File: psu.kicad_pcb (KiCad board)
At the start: 2 copper layers, 76.2 x 76.2 mm, 69 parts, among them J1 Screw_Terminal_01x02, J2 Barrel_Jack, J3 Binding posts, SW1 SW_SP4T, SW2 SW_SP4T, SW3 Lever toggle, U1 LM4040DBZ-2.5, U2 LT3081, U3 LM393, U4 LM334M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

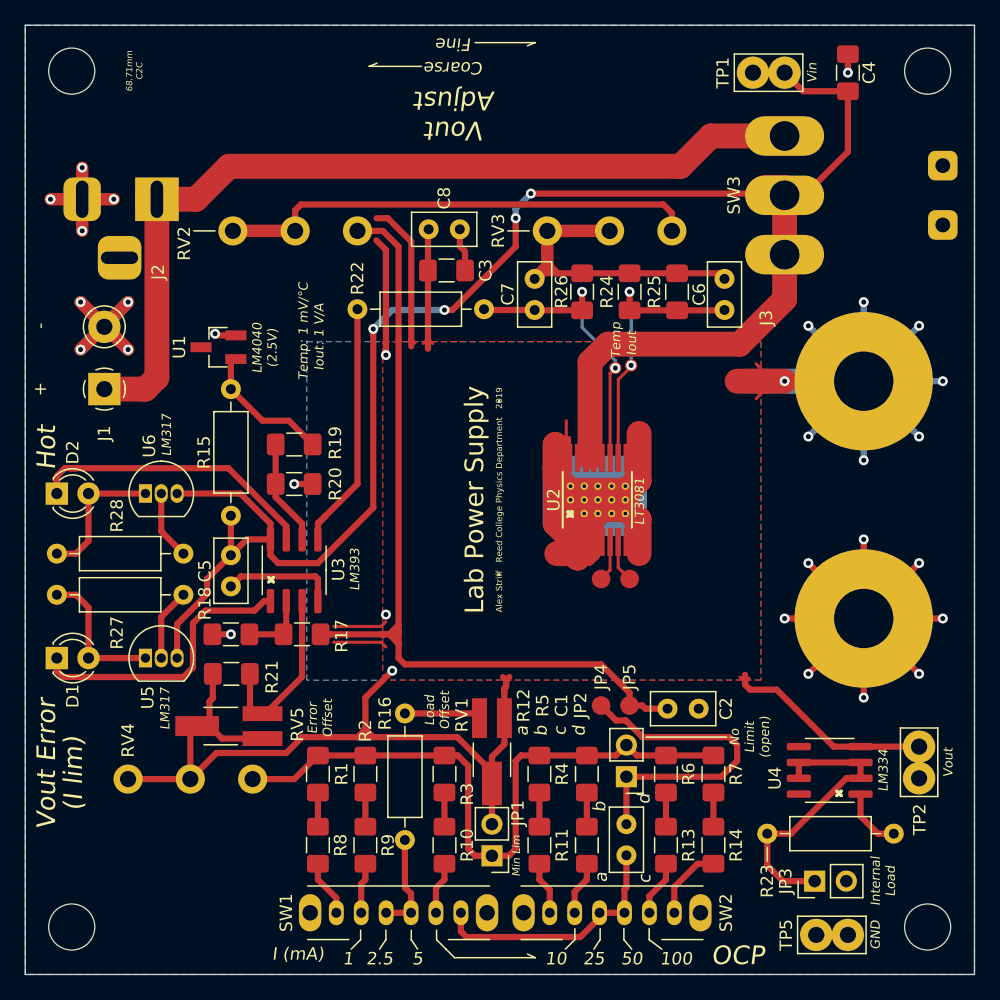
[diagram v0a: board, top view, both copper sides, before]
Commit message: Cleaned up silkscreen
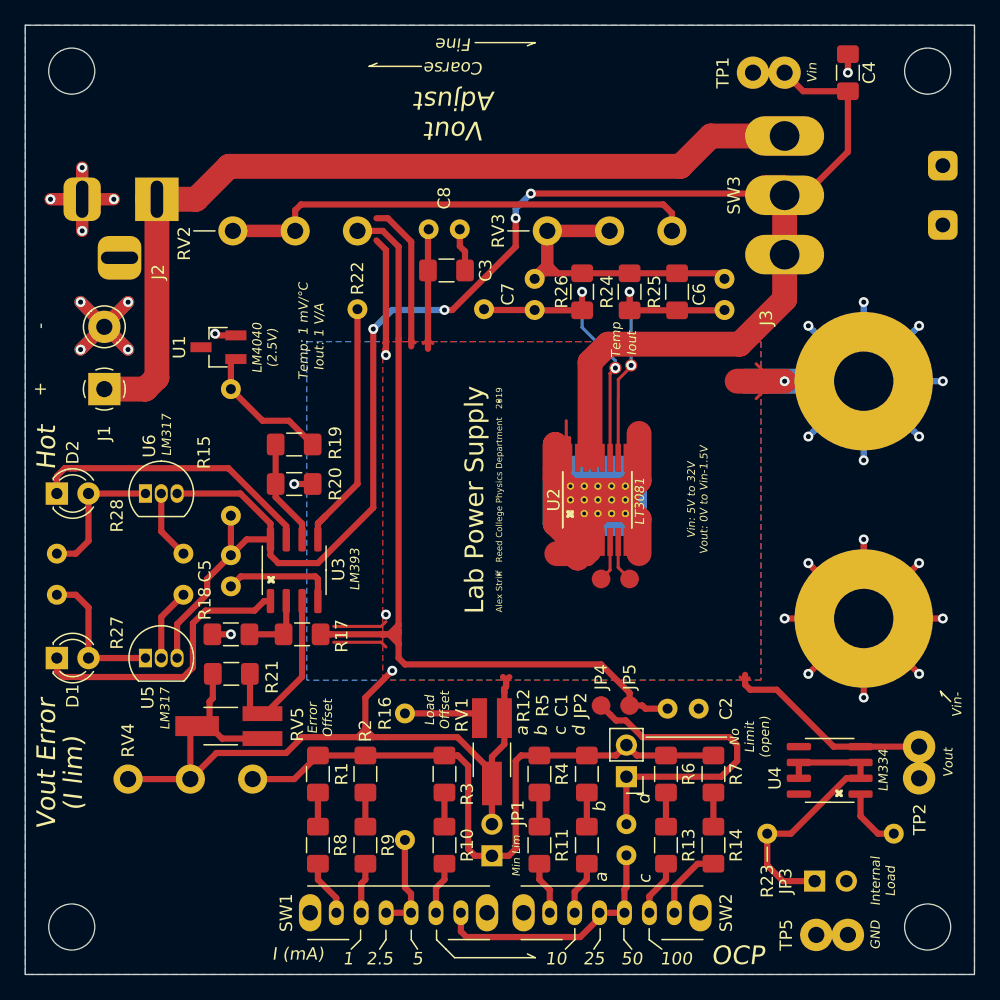
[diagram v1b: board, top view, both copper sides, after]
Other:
- board text added: "Vin-"
- board text added: "Vin: 5V to 32V Vout: 0V to Vin-1.5V"
- board text removed: "68.71mm C2C"

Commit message: Final changes before manufacture
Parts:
- moved C2 0.84 mm to (153.9, 114.8)
- turned J3 to 90 degrees
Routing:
- net Vout: track 313.0 -> 279.4 mm
- net Vin: track 151.6 -> 135.6 mm, vias 4 -> 2
- net GND: track 126.7 -> 119.6 mm, vias 20 -> 21
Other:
- board text removed: "Vin-"

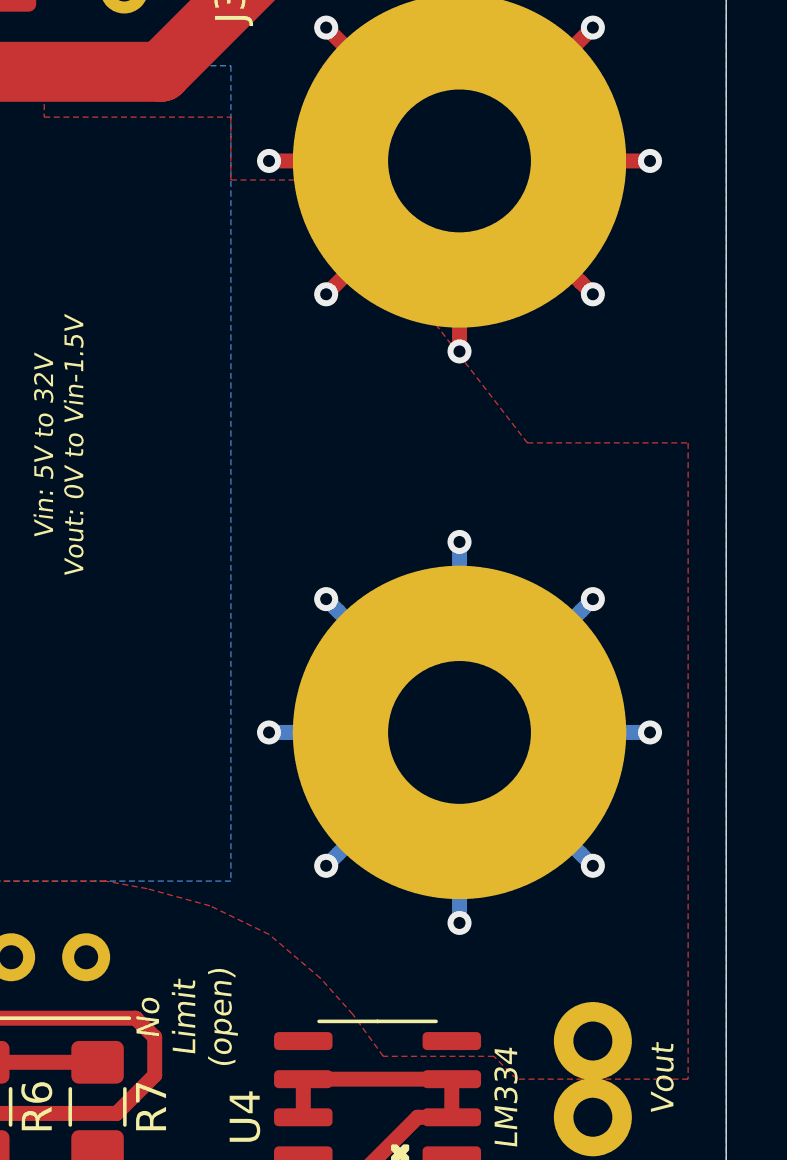
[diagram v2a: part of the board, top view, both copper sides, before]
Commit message: Minor tweak to Vout fill; add gerbers
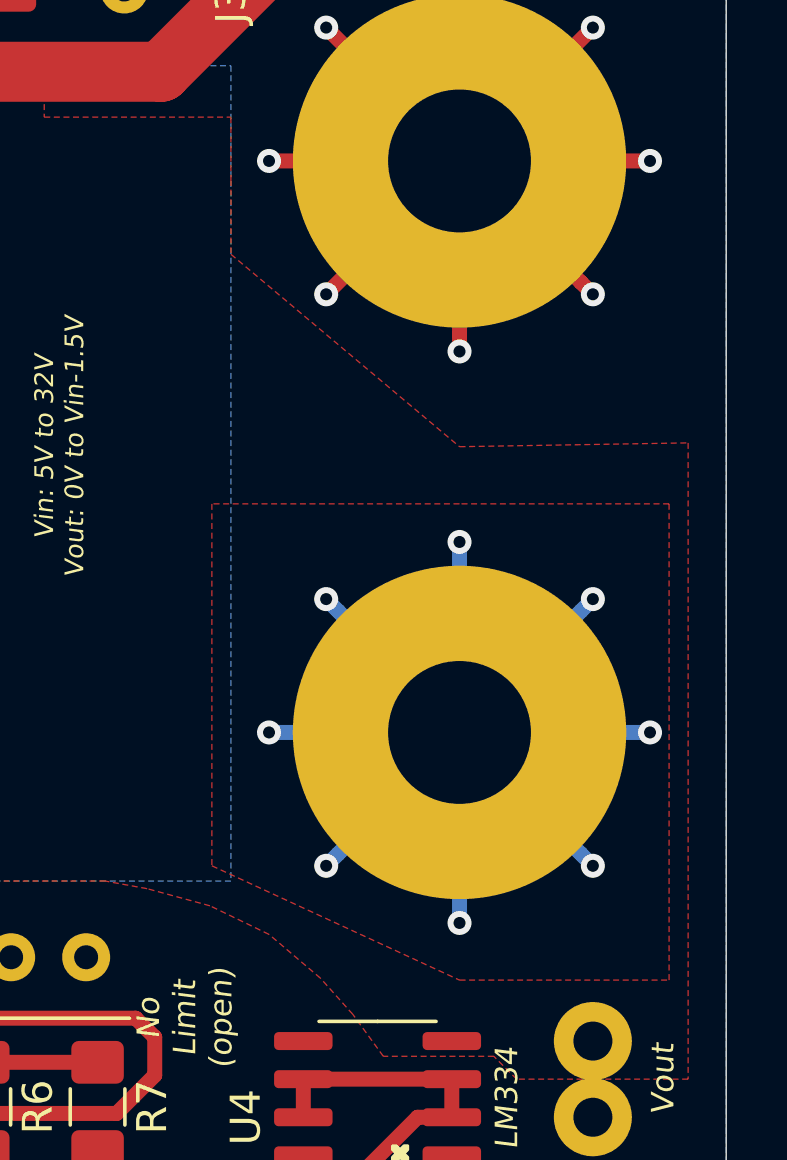
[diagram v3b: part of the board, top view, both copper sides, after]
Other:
- board text added: "NOTES Material: 1.6 mm FR4 (standard); 1 oz copper; 2 layers. Board dimensions: 3 in x 3 in. Colors: White solder mask, black silk screen (front). Surface finish: HASL (with lead) (standard). NO gold fingers NO panelization NO castellated holes NO tented vias NO stencil"
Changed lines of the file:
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@@
   (general
     (thickness 1.6)
-    (drawings 106)
+    (drawings 107)
     (tracks 507)
     (zones 0)
@@
     (visible_elements 7FFFFFFF)
     (pcbplotparams
-      (layerselection 0x010fc_ffffffff)
+      (layerselection 0x012f0_ffffffff)
       (usegerberextensions false)
       (usegerberattributes false)
@@
       (outputformat 1)
       (mirror false)
-      (drillshape 1)
+      (drillshape 0)
       (scaleselection 1)
-      (outputdirectory ""))
+      (outputdirectory "gerbers/"))
   )
   (net 0 "")
@@
     )
   )
+  (gr_text "NOTES\n\nMaterial: 1.6 mm FR4 (standard); 1 oz copper; 2 layers.\nBoard dimensions: 3 in x 3 in.\nColors: White solder mask, black silk screen (front).\nSurface finish: HASL (with lead) (standard).\nNO gold fingers\nNO panelization\nNO castellated holes\nNO tented vias\nNO stencil\n" (at 22.86 40.64) (layer Cmts.User)
+    (effects (font (size 2 2) (thickness 0.15)) (justify left))
+  )
   (gr_circle (center 162.56 97.79) (end 163.449 97.79) (layer B.Mask) (width 0.15))
   (gr_circle (center 165.1 97.79) (end 165.1 97.663) (layer B.Mask) (width 0.15))
@@
     (min_thickness 0.254)
     (keepout (tracks allowed) (vias allowed) (copperpour not_allowed))
-    (fill (arc_segments 32) (thermal_gap 0.508) (thermal_bridge_width 0.508) (smoothing fillet) (radius 2.54))
+    (fill (arc_segments 32) (thermal_gap 0.508) (thermal_bridge_width 0.508))
     (polygon
       (pts
-        (xy 173.99 88.265) (xy 173.99 80.645) (xy 158.75 80.645) (xy 158.75 97.663) (xy 173.99 97.663)
+        (xy 173.99 88.265) (xy 173.99 80.645) (xy 158.75 80.645) (xy 173.99 97.663)
       )
     )
   )
   (zone (net 5) (net_name Vout) (layer F.Cu) (hatch edge 0.508)
+    (priority 1)
     (connect_pads (clearance 0.508))
     (min_thickness 0.254)
-    (fill yes (arc_segments 32) (thermal_gap 0.508) (thermal_bridge_width 0.508) (smoothing fillet) (radius 1.27))
+    (fill yes (arc_segments 32) (thermal_gap 0.508) (thermal_bridge_width 0.508) (smoothing fillet) (radius 2.54))
     (polygon
       (pts
-        (xy 152.527 86.8045) (xy 158.75 86.8045) (xy 158.75 88.9) (xy 161.8615 88.9) (xy 168.628931 97.663)
+        (xy 152.527 86.8045) (xy 158.75 86.8045) (xy 158.75 88.9) (xy 158.75 91.3765) (xy 166.37 97.79)
         (xy 173.99 97.663) (xy 173.99 118.872) (xy 168.275 118.872) (xy 167.513 118.11) (xy 163.83 118.11)
         (xy 162.814 116.713) (xy 161.7345 115.5065) (xy 160.02 114.046) (xy 158.0515 113.0935) (xy 155.956 112.522)
@@
       )
     )
+  )
+  (zone (net 5) (net_name Vout) (layer F.Cu) (hatch edge 0.508)
+    (priority 1)
+    (connect_pads yes (clearance 0.508))
+    (min_thickness 0.254)
+    (fill yes (arc_segments 32) (thermal_gap 0.508) (thermal_bridge_width 0.508))
+    (polygon
+      (pts
+        (xy 166.37 99.695) (xy 158.115 99.695) (xy 158.115 111.76) (xy 166.37 115.57) (xy 173.355 115.57)
+        (xy 173.355 99.695)
+      )
+    )
